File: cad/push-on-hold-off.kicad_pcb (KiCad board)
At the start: 2 copper layers, 22.9 x 12.7 mm, 11 parts, among them P1 CONN_01X04, P2 CONN_01X04, Q1 IRF7309IPBF, SW1 SW_PUSH_SMALL

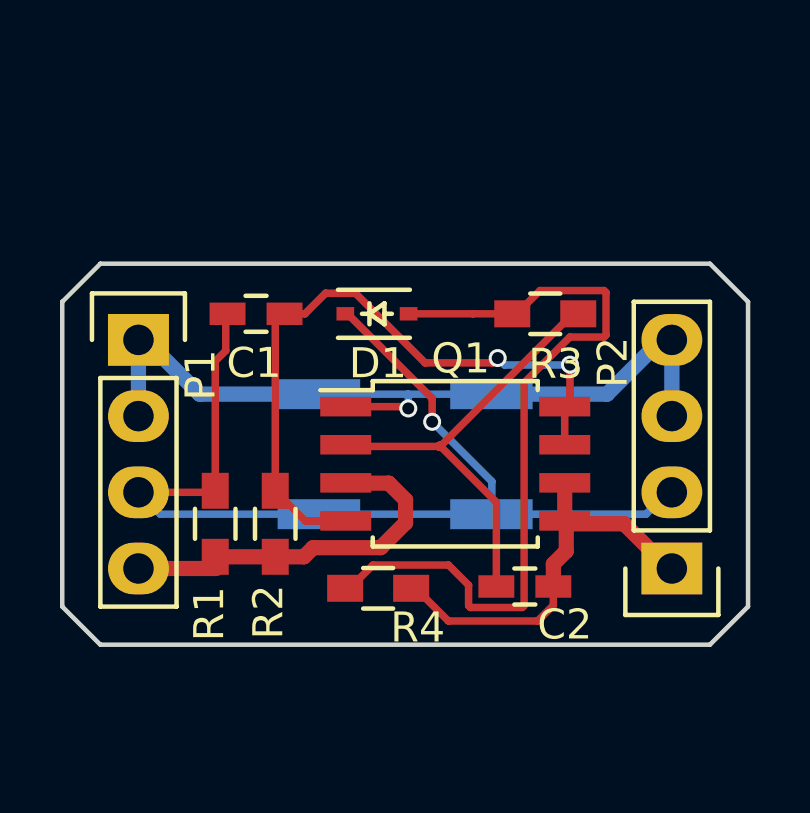
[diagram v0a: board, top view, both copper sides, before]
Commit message: Increase vias to 0.5mm drill with 0.7mm pad
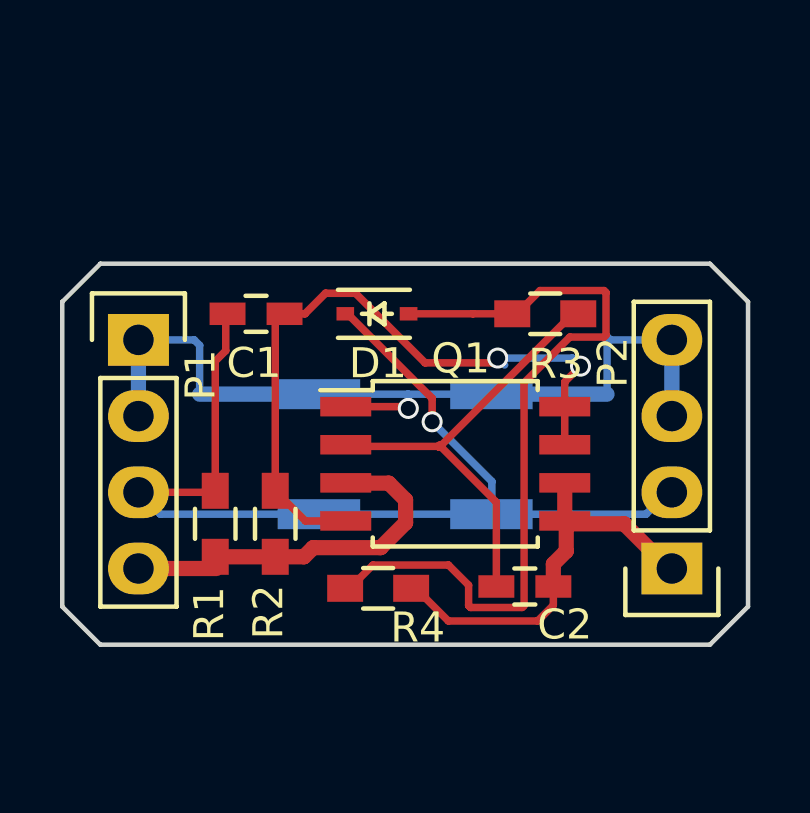
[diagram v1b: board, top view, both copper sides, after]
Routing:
- net GND: track 28.0 -> 30.9 mm
- net Net-(C1-Pad1): track 22.9 -> 23.8 mm
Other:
- net class Default: via_dia 0.6 -> 0.7; via_drill 0.4 -> 0.5
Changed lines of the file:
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@@
-(kicad_pcb (version 4) (host pcbnew 0.201509051501+6156~29~ubuntu14.04.1-product)
+(kicad_pcb (version 4) (host pcbnew no-vcs-found-product)
   (general
     (links 27)
@@
     (thickness 1.6)
     (drawings 16)
-    (tracks 128)
+    (tracks 133)
     (zones 0)
     (modules 11)
@@
   (page A4)
   (layers
-    (0 F.Cu signal hide)
+    (0 F.Cu signal)
     (31 B.Cu signal)
     (32 B.Adhes user)
@@
     (segment_width 0.2)
     (edge_width 0.15)
-    (via_size 0.6)
-    (via_drill 0.4)
+    (via_size 0.7)
+    (via_drill 0.5)
     (via_min_size 0.4)
     (via_min_drill 0.3)
@@
     (aux_axis_origin 0 0)
     (grid_origin 217.175 100.345)
-    (visible_elements 7FFFBFFF)
+    (visible_elements 7FFFFFFF)
     (pcbplotparams
       (layerselection 0x010f0_80000001)
@@
     (clearance 0.2)
     (trace_width 0.25)
-    (via_dia 0.6)
-    (via_drill 0.4)
+    (via_dia 0.7)
+    (via_drill 0.5)
     (uvia_dia 0.3)
     (uvia_drill 0.1)
@@
     (effects (font (size 1 1) (thickness 0.25)) (justify mirror))
   )
-  (gr_text BUT (at 233.685 107.965) (layer B.SilkS)
-    (effects (font (size 1 1) (thickness 0.25)) (justify mirror))
-  )
-  (gr_text GND (at 233.685 105.425) (layer B.SilkS)
-    (effects (font (size 1 1) (thickness 0.25)) (justify mirror))
-  )
-  (gr_text GND (at 233.431 102.885) (layer B.SilkS)
+  (gr_text BUT (at 233.575 107.945) (layer B.SilkS)
+    (effects (font (size 1 1) (thickness 0.25)) (justify mirror))
+  )
+  (gr_text GND (at 233.475 105.445) (layer B.SilkS)
+    (effects (font (size 1 1) (thickness 0.25)) (justify mirror))
+  )
+  (gr_text GND (at 233.375 102.745) (layer B.SilkS)
     (effects (font (size 1 1) (thickness 0.25)) (justify mirror))
   )
@@
     (effects (font (size 1 1) (thickness 0.25)) (justify mirror))
   )
-  (gr_text BUT (at 221.239 107.965) (layer B.SilkS)
-    (effects (font (size 1 1) (thickness 0.25)) (justify mirror))
-  )
-  (gr_text GND (at 221.335 105.435) (layer B.SilkS)
-    (effects (font (size 1 1) (thickness 0.25)) (justify mirror))
-  )
-  (gr_text GND (at 221.355 102.875) (layer B.SilkS)
+  (gr_text BUT (at 221.275 108.045) (layer B.SilkS)
+    (effects (font (size 1 1) (thickness 0.25)) (justify mirror))
+  )
+  (gr_text GND (at 221.375 105.445) (layer B.SilkS)
+    (effects (font (size 1 1) (thickness 0.25)) (justify mirror))
+  )
+  (gr_text GND (at 221.375 102.845) (layer B.SilkS)
     (effects (font (size 1 1) (thickness 0.25)) (justify mirror))
   )
@@
   (gr_line (start 215.9 101.6) (end 215.9 111.76) (angle 90) (layer Edge.Cuts) (width 0.15))
   (gr_line (start 217.17 100.33) (end 215.9 101.6) (angle 90) (layer Edge.Cuts) (width 0.15))
-  (segment (start 232.65 105.095) (end 232.65 106.38) (width 0.254) (layer F.Cu) (net 1))
-  (segment (start 232.65 106.38) (end 232.685 106.415) (width 0.254) (layer F.Cu) (net 1))
-  (segment (start 232.685 106.415) (end 232.65 106.365) (width 0.254) (layer F.Cu) (net 1))
+  (segment (start 232.65 105.095) (end 232.65 104.27) (width 0.25) (layer F.Cu) (net 1))
+  (segment (start 232.905 103.475) (end 230.415 103.475) (width 0.25) (layer B.Cu) (net 1))
+  (segment (start 233.175 103.745) (end 232.905 103.475) (width 0.25) (layer B.Cu) (net 1))
+  (via (at 233.175 103.745) (size 0.7) (drill 0.5) (layers F.Cu B.Cu) (net 1))
+  (segment (start 232.65 104.27) (end 233.175 103.745) (width 0.25) (layer F.Cu) (net 1))
   (segment (start 223.31 102) (end 223.99 102) (width 0.254) (layer F.Cu) (net 1))
-  (segment (start 232.825 103.695) (end 232.825 105.055) (width 0.254) (layer F.Cu) (net 1))
-  (via (at 232.825 103.695) (size 0.6) (drill 0.4) (layers F.Cu B.Cu) (net 1))
-  (segment (start 232.815 103.705) (end 232.825 103.695) (width 0.254) (layer B.Cu) (net 1))
-  (segment (start 230.645 103.705) (end 232.815 103.705) (width 0.254) (layer B.Cu) (net 1))
-  (segment (start 230.415 103.475) (end 230.645 103.705) (width 0.254) (layer B.Cu) (net 1))
-  (via (at 230.415 103.475) (size 0.6) (drill 0.4) (layers F.Cu B.Cu) (net 1))
+  (via (at 230.415 103.475) (size 0.7) (drill 0.5) (layers F.Cu B.Cu) (net 1))
   (segment (start 230.255 103.635) (end 230.415 103.475) (width 0.254) (layer F.Cu) (net 1))
   (segment (start 227.995 103.635) (end 230.255 103.635) (width 0.254) (layer F.Cu) (net 1))
@@
   (segment (start 224.675 101.315) (end 225.675 101.315) (width 0.254) (layer F.Cu) (net 1))
   (segment (start 223.99 102) (end 224.675 101.315) (width 0.254) (layer F.Cu) (net 1))
+  (segment (start 230.415 103.475) (end 230.645 103.705) (width 0.254) (layer B.Cu) (net 1))
+  (segment (start 232.65 105.095) (end 232.65 106.38) (width 0.254) (layer F.Cu) (net 1))
+  (segment (start 232.65 106.38) (end 232.685 106.415) (width 0.254) (layer F.Cu) (net 1))
+  (segment (start 232.685 106.415) (end 232.65 106.365) (width 0.254) (layer F.Cu) (net 1))
   (segment (start 232.825 105.055) (end 232.65 105.095) (width 0.254) (layer F.Cu) (net 1))
   (segment (start 225.35 108.905) (end 224.005 108.905) (width 0.254) (layer F.Cu) (net 1))
@@
   (segment (start 225.41 102) (end 228.23 104.82) (width 0.254) (layer F.Cu) (net 2))
   (segment (start 228.23 104.82) (end 228.23 105.6) (width 0.254) (layer F.Cu) (net 2))
-  (via (at 228.23 105.6) (size 0.6) (drill 0.4) (layers F.Cu B.Cu) (net 2))
+  (via (at 228.23 105.6) (size 0.7) (drill 0.5) (layers F.Cu B.Cu) (net 2))
   (segment (start 228.23 105.6) (end 230.22 107.59) (width 0.254) (layer B.Cu) (net 2))
   (segment (start 230.22 107.59) (end 230.22 108.4) (width 0.254) (layer B.Cu) (net 2))
@@
   (segment (start 230.87 102) (end 230.94 101.93) (width 0.25) (layer F.Cu) (net 5))
   (segment (start 230.94 101.93) (end 230.9 102) (width 0.25) (layer F.Cu) (net 5))
+  (segment (start 234.06 104.68) (end 234.06 102.76) (width 0.25) (layer B.Cu) (net 6))
+  (segment (start 230.205 104.68) (end 234.06 104.68) (width 0.508) (layer B.Cu) (net 6))
+  (segment (start 234.17 102.87) (end 236.22 102.87) (width 0.25) (layer B.Cu) (net 6) (status 800000))
+  (segment (start 234.06 102.76) (end 234.17 102.87) (width 0.25) (layer B.Cu) (net 6))
+  (segment (start 220.48 104.68) (end 220.48 103.05) (width 0.25) (layer B.Cu) (net 6))
+  (segment (start 224.455 104.68) (end 220.48 104.68) (width 0.508) (layer B.Cu) (net 6))
+  (segment (start 220.3 102.87) (end 218.44 102.87) (width 0.25) (layer B.Cu) (net 6))
+  (segment (start 220.48 103.05) (end 220.3 102.87) (width 0.25) (layer B.Cu) (net 6))
   (segment (start 227.435 105.155) (end 227.435 104.705) (width 0.25) (layer B.Cu) (net 6))
-  (via (at 227.435 105.155) (size 0.6) (drill 0.4) (layers F.Cu B.Cu) (net 6))
+  (via (at 227.435 105.155) (size 0.7) (drill 0.5) (layers F.Cu B.Cu) (net 6))
   (segment (start 225.35 105.095) (end 227.375 105.095) (width 0.25) (layer F.Cu) (net 6))
   (segment (start 227.375 105.095) (end 227.435 105.155) (width 0.25) (layer F.Cu) (net 6))
@@
   (segment (start 236.22 105.52) (end 236.26 105.56) (width 0.25) (layer B.Cu) (net 6))
   (segment (start 236.26 105.56) (end 236.22 105.41) (width 0.25) (layer B.Cu) (net 6))
-  (segment (start 230.205 104.68) (end 234.06 104.68) (width 0.508) (layer B.Cu) (net 6))
-  (segment (start 234.06 104.68) (end 235.84 102.9) (width 0.508) (layer B.Cu) (net 6))
   (segment (start 235.84 102.9) (end 235.9 102.9) (width 0.25) (layer B.Cu) (net 6))
   (segment (start 235.9 102.9) (end 235.92 102.88) (width 0.25) (layer B.Cu) (net 6))
@@
   (segment (start 218.44 105.45) (end 218.53 105.54) (width 0.25) (layer B.Cu) (net 6))
   (segment (start 218.53 105.54) (end 218.44 105.41) (width 0.25) (layer B.Cu) (net 6))
-  (segment (start 224.455 104.68) (end 220.48 104.68) (width 0.508) (layer B.Cu) (net 6))
-  (segment (start 220.48 104.68) (end 218.75 102.95) (width 0.508) (layer B.Cu) (net 6))
   (segment (start 218.75 102.95) (end 218.44 102.87) (width 0.25) (layer B.Cu) (net 6))
   (segment (start 227.345 108.965) (end 227.345 108.205) (width 0.508) (layer F.Cu) (net 7))

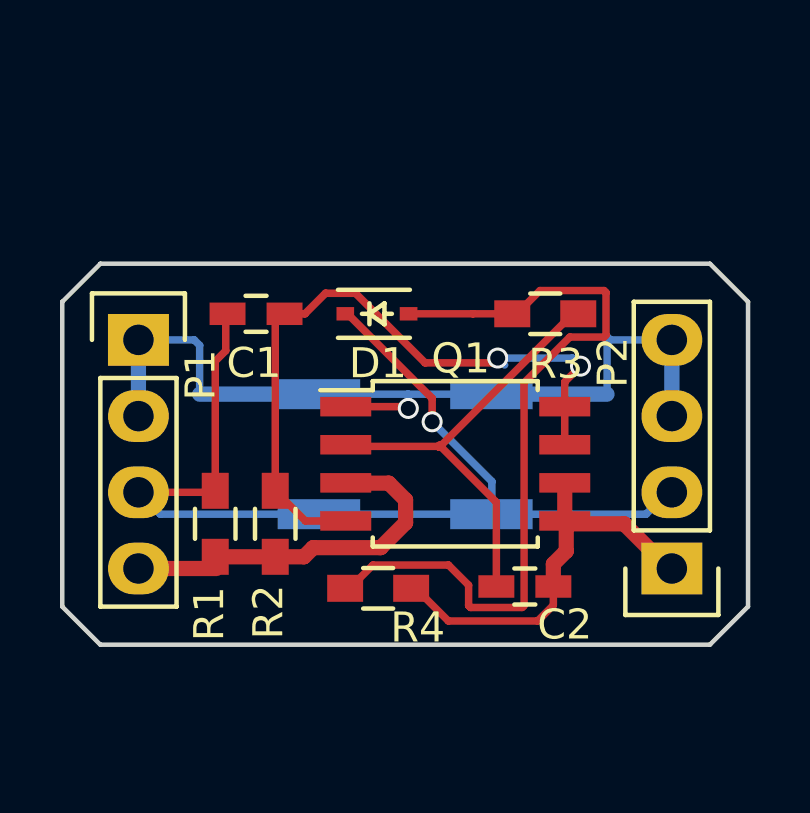
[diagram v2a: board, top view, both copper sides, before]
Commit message: Switch button footprint to match BOM
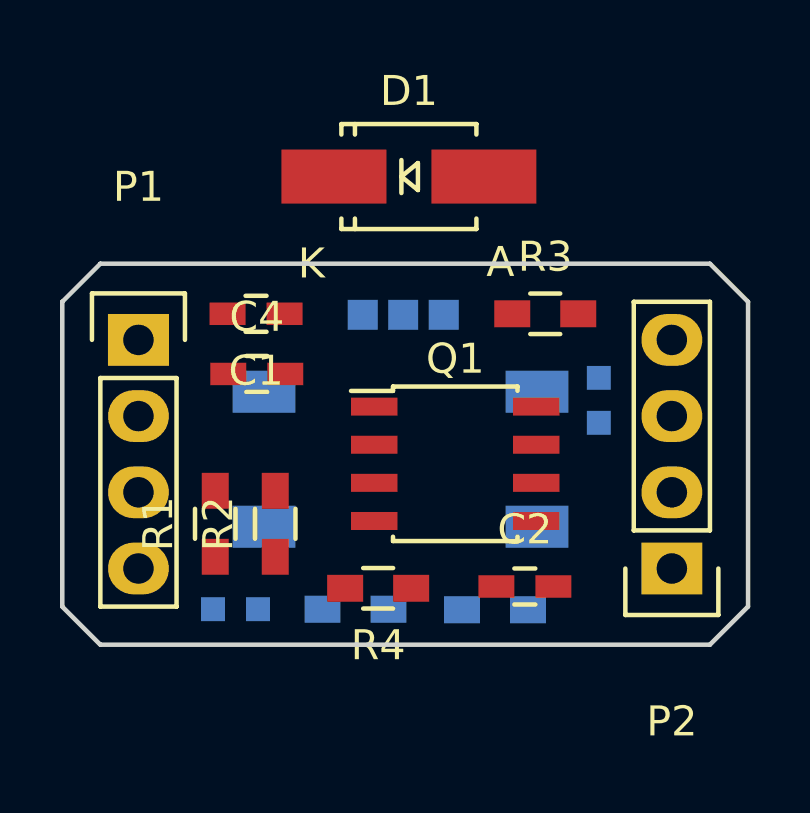
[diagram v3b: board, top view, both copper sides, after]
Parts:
- added C4: 0.1uF, KiCad/Capacitors_SMD.pretty:C_0603_HandSoldering, F.Cu at (222.4, 104.0)
- added JP1: JUMPER3, mcous/kicad-lib/footprints/jumper.pretty:SOLDER-JUMPER_2-WAY, B.Cu at (227.3, 102.0)
- added LED1: LED, KiCad/LEDs.pretty:LED_0603, B.Cu at (221.7, 111.8)
- added LED2: LED, KiCad/LEDs.pretty:LED_0603, B.Cu at (233.8, 104.9)
- added R5: 1k, KiCad/Resistors_SMD.pretty:R_0603_HandSoldering, B.Cu at (225.7, 111.8)
- added R6: 1k, KiCad/Resistors_SMD.pretty:R_0603_HandSoldering, B.Cu at (230.3, 111.9)
- C1, C2: footprint Capacitors_SMD.pretty:C_0603_HandSoldering -> KiCad/Capacitors_SMD.pretty:C_0603_HandSoldering
- D1: footprint Diodes_SMD.pretty:SOD-323 -> KiCad/Diodes_SMD.pretty:SMA_Handsoldering
- P1, P2: footprint Pin_Headers.pretty:Pin_Header_Straight_1x04 -> KiCad/Pin_Headers.pretty:Pin_Header_Straight_1x04
- Q1: footprint Housings_SOIC.pretty:SOIJ-8_5.3x5.3mm_Pitch1.27mm -> Housings_SOIC:SOIC-8_3.9x4.9mm_Pitch1.27mm
- R1, R2, R3, R4: footprint Resistors_SMD.pretty:R_0603_HandSoldering -> KiCad/Resistors_SMD.pretty:R_0603_HandSoldering
- SW1: footprint Buttons_Switches_SMD.pretty:SW_SPST_EVPBF -> custom:FSM2JSMA
- moved D1 4.70 mm to (227.5, 97.4)
- moved SW1 0.23 mm to (227.2, 106.8), turned to 270 degrees
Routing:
- net /Button: track 35.9 -> 0.00 mm, vias 1 -> 0
- net GND: track 30.9 -> 0.00 mm, vias 1 -> 0
- net Net-(D1-Pad2): track 26.6 -> 0.00 mm
- net Net-(C1-Pad1): track 23.8 -> 0.00 mm, vias 2 -> 0
- net Net-(C2-Pad1): track 15.2 -> 0.00 mm
- net /Vout: track 13.9 -> 0.00 mm
- net /Vin: track 13.6 -> 0.00 mm

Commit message: Sort button-side of board
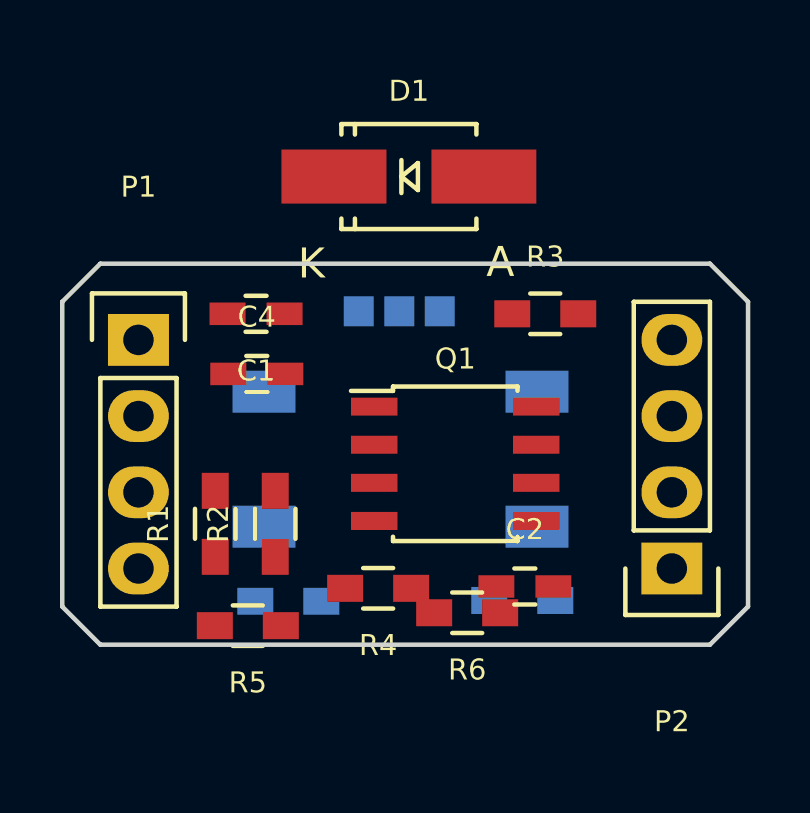
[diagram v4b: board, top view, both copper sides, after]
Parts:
- LED1, LED2: footprint KiCad/LEDs.pretty:LED_0603 -> KiCad/Resistors_SMD.pretty:R_0603_HandSoldering
- Q1: footprint Housings_SOIC:SOIC-8_3.9x4.9mm_Pitch1.27mm -> KiCad/Housings_SOIC.pretty:SOIC-8_3.9x4.9mm_Pitch1.27mm
- R5, R6: moved to F.Cu
- moved LED2 7.14 mm to (231.2, 111.6), turned to 180 degrees
- moved R5 3.63 mm to (222.1, 112.4)
- moved LED1 1.78 mm to (223.4, 111.6)
- moved R6 0.93 mm to (229.4, 112.0), turned to 180 degrees
- moved JP1 0.18 mm to (227.1, 101.9)
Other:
- board text added: "BTN"
- board text added: "auto"
- board text added: "off"
- board text added: "on"
- board text removed: "BUT"

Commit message: Switch diode to a mini-melf
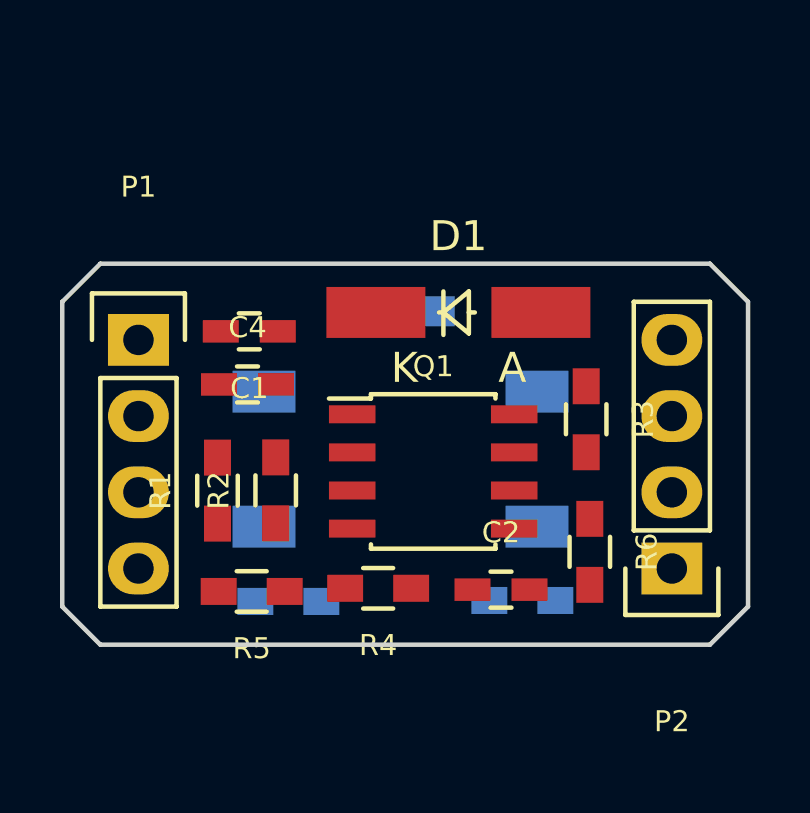
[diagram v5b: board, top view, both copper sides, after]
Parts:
- D1: footprint KiCad/Diodes_SMD.pretty:SMA_Handsoldering -> KiCad/Diodes_SMD.pretty:MiniMELF_Handsoldering
- moved D1 4.82 mm to (229.1, 102.0)
- moved R6 4.56 mm to (233.5, 109.9), turned to 270 degrees
- moved R3 3.77 mm to (233.4, 105.5), turned to 270 degrees
- moved R5 1.15 mm to (222.2, 111.3)
- moved R2 1.12 mm to (223.0, 107.9)
- moved R1 1.11 mm to (221.1, 107.9)
- moved C2 0.80 mm to (230.5, 111.2)
- moved Q1 0.78 mm to (228.3, 107.3)
- moved C1 0.63 mm to (222.1, 102.6)
- moved C4 0.47 mm to (222.1, 104.4)

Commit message: Route the board
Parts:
- moved LED2 0.77 mm to (230.5, 111.6), turned to 0 degrees
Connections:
- C4 pad 1: /Vin -> Net-(C4-Pad1)
- JP1 pad 2: /Vin -> Net-(C4-Pad1)
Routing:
- net GND: track 0.00 -> 40.5 mm, vias 0 -> 1
- net Net-(C1-Pad1): track 0.00 -> 28.8 mm, vias 0 -> 3
- net /Button: track 0.00 -> 24.5 mm
- net /Vin: track 0.00 -> 19.7 mm, vias 0 -> 3
- net /Vout: track 0.00 -> 16.2 mm
- net Net-(D1-Pad2): track 0.00 -> 14.9 mm
- net Net-(C4-Pad1): track 0.00 -> 13.8 mm, vias 0 -> 1
- net Net-(C2-Pad1): track 0.00 -> 13.7 mm, vias 0 -> 4
- net Net-(LED2-Pad2): track 0.00 -> 3.77 mm, vias 0 -> 1
- net Net-(LED1-Pad2): track 0.00 -> 3.06 mm, vias 0 -> 1

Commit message: Sort out silkscreen and plot
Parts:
- moved R5 0.10 mm to (222.2, 111.2)
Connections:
- C4 pad 1: Net-(C4-Pad1) -> /Vin
- JP1 pad 2: Net-(C4-Pad1) -> /Vin
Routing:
- net /Vin: track 19.7 -> 36.3 mm, vias 3 -> 4
- net GND: track 40.5 -> 25.2 mm
- net Net-(C4-Pad1): track 13.8 -> 0.00 mm, vias 1 -> 0
- net /Vout: track 16.2 -> 17.1 mm
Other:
- rule trace_min: 0.2 -> 0.1
